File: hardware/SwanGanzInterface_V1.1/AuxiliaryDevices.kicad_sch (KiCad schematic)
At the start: 28 parts, among them J10 Conn_01x04_Pin, J11 Conn_01x07_Pin, J8 Conn_01x04_Pin, J9 1051640001, U11 FT232RNL, U14 TSC2046IPWR

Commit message: Digital Traces
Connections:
- net MSP_RX_PA9_FT232_TX is gone; now on net MSP_RX_PA1_FT_TX: J10.2 (Pin_2)
- net MSP_TX_PA8_FT232_RX is gone; now on net MSP_TX_PA28_FT_RX: J10.3 (Pin_3)
- net GND: now also R44.1; no longer R44.2
- net USB_CONN_PA30 renamed USB_CONN_PA7
- net USB_CONN_PA7: now also R44.2; no longer R44.1
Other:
- moved on the sheet: J10, R43, R44

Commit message: SGI v2 Layout Complete
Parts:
- R48: renamed from R44; value 19.412k -> 19.1k
- renumbered C27 to C29, C28 to C30, C29 to C31, C30 to C32, C31 to C33, C37 to C34, J9 to J10, J10 to J11, J11 to J12, J8 to J9, R36 to R40, R37 to R41, R38 to R42, R39 to R43, R40 to R44, R41 to R45, R42 to R46, R43 to R47, R45 to R49, U11 to U12, U14 to U13

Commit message: Finished selecting parts for bom, changed resistor values for leds
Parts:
- R41, R43: value 2k -> 1k
- R44: value 2k -> 1.8k
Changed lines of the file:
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@@
 			)
 		)
-		(property "Value" "2k"
-			(at 151.638 163.576 90)
+		(property "Value" "1k"
+			(at 151.638 163.322 90)
 			(effects
 				(font
@@
 			)
 		)
-		(property "Value" "2k"
+		(property "Value" "1k"
 			(at 138.938 163.576 90)
 			(effects
@@
 			)
 		)
-		(property "Value" "2k"
-			(at 163.068 163.322 90)
+		(property "Value" "1.8k"
+			(at 163.068 164.084 90)
 			(effects
 				(font

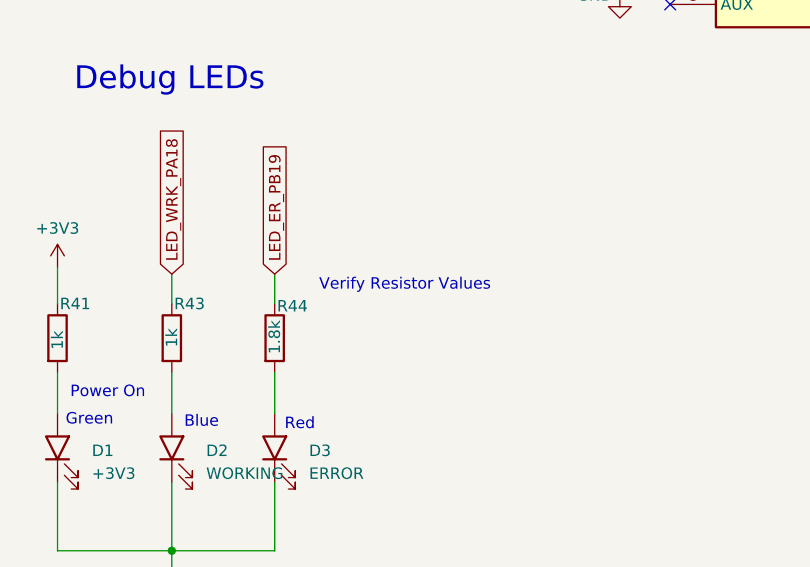
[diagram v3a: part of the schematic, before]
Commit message: Bom changes - purchase request sent
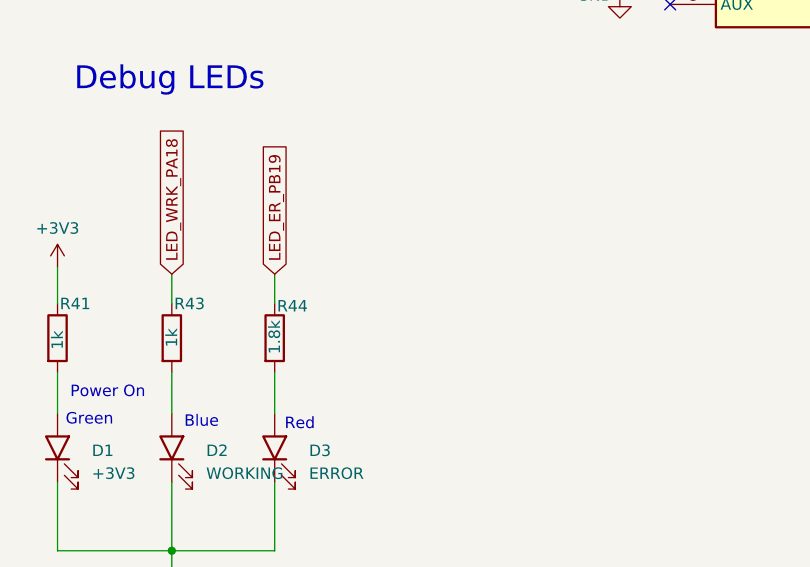
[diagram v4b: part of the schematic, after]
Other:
- note removed: "Verify Resistor Values"
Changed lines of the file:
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@@
-		)
-	)
-	(text "Verify Resistor Values"
-		(exclude_from_sim no)
-		(at 177.546 156.464 0)
-		(effects
-			(font
-				(size 1.27 1.27)
-			)
 		)
 	)
